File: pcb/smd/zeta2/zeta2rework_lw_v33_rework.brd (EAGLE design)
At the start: 81 x 50.2 mm, 100 parts, among them IC1 DRV8844PWPR, IC2 DRV8844PWPR, J1 UJ2-MIBH2-4-SMT-TR, M1 IRLML2502, M2 IRLML2502, M3 IRLML2502, U1 STM32F427VI, U3 ICM-20948, U5 DS18B20U+

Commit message: progress on traces
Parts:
- removed D2: BAT60JFILM, BAT60JFILM:SOD2513X117N
- removed J1: UJ2-MIBH2-4-SMT-TR, UJ2-MIBH2-4-SMT-TR:CUI_UJ2-MIBH2-4-SMT-TR
- removed R12: 1k5, rcl:R0603
- removed R14, R18: 22r, rcl:R0603
- removed R16: 100k, rcl:R0603
- removed R19: 100r, rcl:R0603
- removed SJ2: (no value), jumper:SJ
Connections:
- removed net N$15: D2.2, J1.1
- removed net N$17: J1.4, R16.2
- removed net N$25: R19.1, SJ2.2
- removed net N$34: J1.2, R14.2
- removed net N$40: J1.SH1, J1.SH2, J1.SH3, J1.SH4, J1.SH5, R19.2
- removed net N$5: J1.3, R12.1, R18.2
- net +3V3: no longer R12.2
- net +5V: no longer D2.1
- net GND: no longer J1.5, SJ2.1
- net USB_OTG_DM: no longer R14.1
- net USB_OTG_DP: no longer R18.1
- net USB_OTG_ID: no longer R16.1
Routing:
- net N$17: track 5.79 -> 0.00 mm
- net N$5: track 5.68 -> 0.00 mm
- net N$15: track 5.33 -> 0.00 mm
- net GND: track 226.3 -> 221.6 mm, vias 113 -> 111
- net N$34: track 3.93 -> 0.00 mm
- added copper zone on layer 1, net +3V3

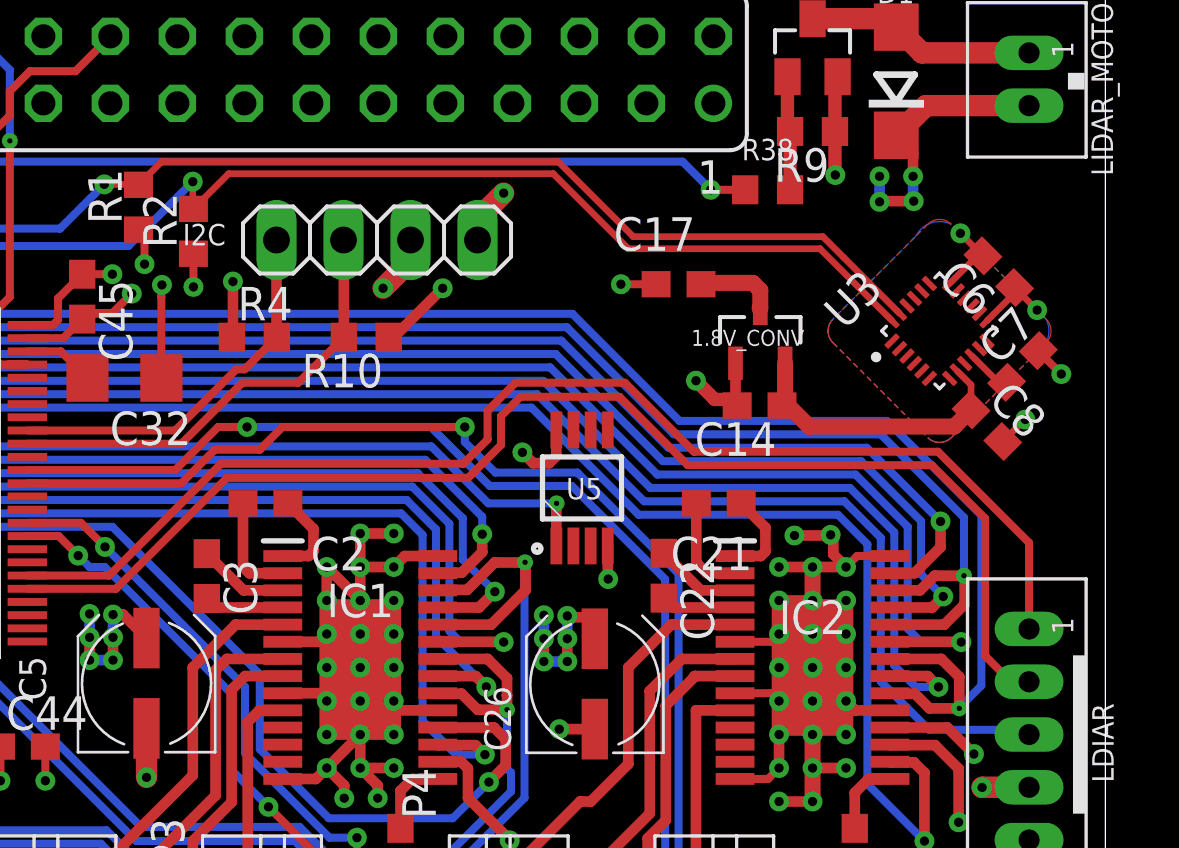
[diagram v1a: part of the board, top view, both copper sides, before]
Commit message: connected power supply
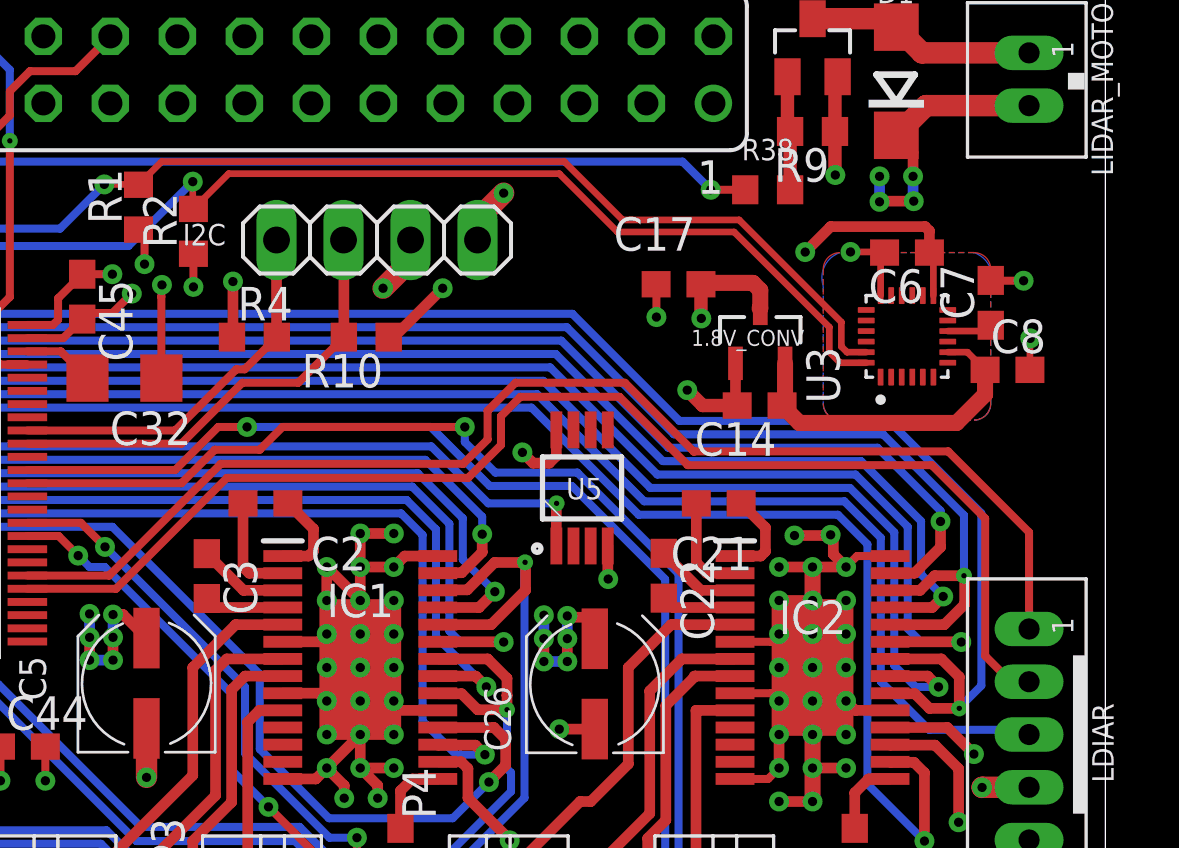
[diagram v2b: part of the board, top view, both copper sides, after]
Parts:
- moved C6 3.55 mm to (73.4, 44.9), turned to 180 degrees
- moved C7 2.69 mm to (76.6, 43.0), turned to 90 degrees
- moved C8 2.26 mm to (77.2, 40.5), turned to 0 degrees
- moved U3 1.25 mm to (73.4, 41.8), turned to 90 degrees
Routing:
- net +3V3: track 96.2 -> 102.4 mm, vias 26 -> 27
- net +1.8V: track 11.3 -> 12.9 mm
